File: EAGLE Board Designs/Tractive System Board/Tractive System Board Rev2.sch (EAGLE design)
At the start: 135 parts, among them J3 CONNECTOR-8_S_S, J5 CONNECTOR-4__, K4 RELAY_SPST_NC_POLARIZED_3550_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, K5 RELAY_SPST_NO_3550_12, Q2 TRANSISTOR_N_MOS__PMV15ENEA, U1 LTC6994_1, U10 DCM4623TD2J13D0T70, U11 RELAY_SOLIDSTATE_NC_AG, U15 LOGICGATE_INVERTER_DCKR, U16 LTC3639, U17 VOLTAGE_REGULATOR_ADJ_LR8_DPAK, U18 ISO224B_AIRGAP, U19 ISO224B_AIRGAP, U2 VOLTAGE_REGULATOR_SOT223_5V

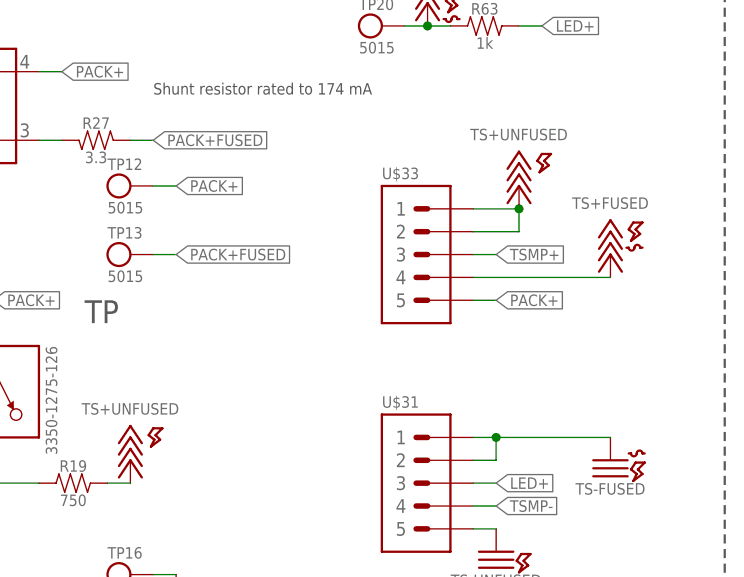
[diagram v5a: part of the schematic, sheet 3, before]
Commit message: Fixed molex connectors
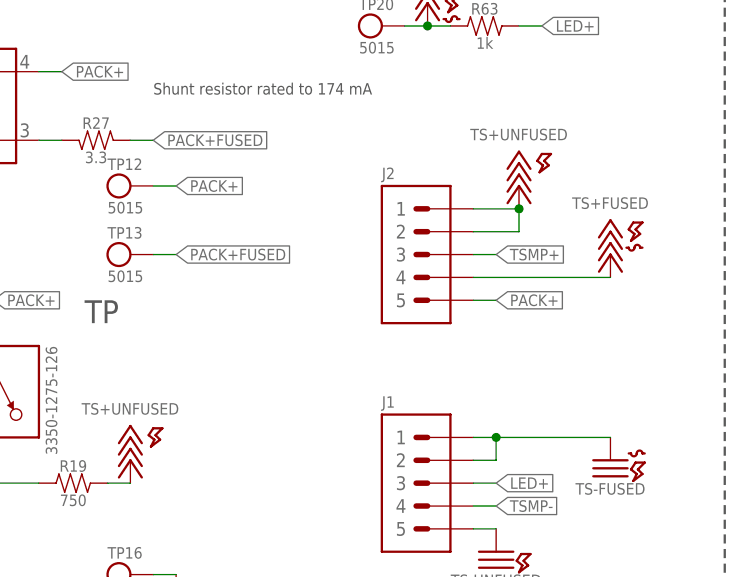
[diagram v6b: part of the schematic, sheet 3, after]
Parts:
- renumbered U$31 to J1, U$33 to J2
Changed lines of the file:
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@@
 <part name="U$3" library="HyTechSupplies" deviceset="TS-FUSED" device=""/>
 <part name="U$30" library="HyTechSupplies" deviceset="TS-FUSED" device=""/>
-<part name="U$31" library="HyTechDevices" deviceset="CONNECTOR-5_?_*" device="MICRO_V6S"/>
-<part name="U$33" library="HyTechDevices" deviceset="CONNECTOR-5_?_*" device="MICRO_V7S"/>
+<part name="J1" library="HyTechDevices" deviceset="CONNECTOR-5_?_*" device="MICRO_V6S"/>
+<part name="J2" library="HyTechDevices" deviceset="CONNECTOR-5_?_*" device="MICRO_V7S"/>
 <part name="P18" library="HyTechSupplies" deviceset="+5V" device=""/>
 <part name="TP16" library="HyTechDevices" deviceset="TEST_POINT" device=""/>
@@
 <attribute name="VALUE" x="256.54" y="147.32" size="1.27" layer="96" align="top-center"/>
 </instance>
-<instance part="U$31" gate="G$1" x="231.14" y="154.94" smashed="yes">
+<instance part="J1" gate="G$1" x="231.14" y="154.94" smashed="yes">
 <attribute name="NAME" x="231.14" y="155.702" size="1.27" layer="95"/>
 </instance>
-<instance part="U$33" gate="G$1" x="231.14" y="180.34" smashed="yes">
+<instance part="J2" gate="G$1" x="231.14" y="180.34" smashed="yes">
 <attribute name="NAME" x="231.14" y="181.102" size="1.27" layer="95"/>
 </instance>
@@
 <pinref part="P14" gate="G$1" pin="TS+UNFUSED"/>
 <wire x1="241.3" y1="177.8" x2="246.38" y2="177.8" width="0.6096" layer="91"/>
-<pinref part="U$33" gate="G$1" pin="1"/>
-<pinref part="U$33" gate="G$1" pin="2"/>
+<pinref part="J2" gate="G$1" pin="1"/>
+<pinref part="J2" gate="G$1" pin="2"/>
 <wire x1="241.3" y1="175.26" x2="246.38" y2="175.26" width="0.1524" layer="91"/>
 <wire x1="246.38" y1="175.26" x2="246.38" y2="177.8" width="0.1524" layer="91"/>
@@
 <wire x1="241.3" y1="167.64" x2="243.84" y2="167.64" width="0.6096" layer="91"/>
 <label x="243.84" y="167.64" size="1.27" layer="95" xref="yes"/>
-<pinref part="U$33" gate="G$1" pin="5"/>
+<pinref part="J2" gate="G$1" pin="5"/>
 </segment>
 <segment>
@@
 <wire x1="241.3" y1="172.72" x2="243.84" y2="172.72" width="0.6096" layer="91"/>
 <label x="243.84" y="172.72" size="1.27" layer="95" xref="yes"/>
-<pinref part="U$33" gate="G$1" pin="3"/>
+<pinref part="J2" gate="G$1" pin="3"/>
 </segment>
 <segment>
@@
 <wire x1="241.3" y1="144.78" x2="243.84" y2="144.78" width="0.6096" layer="91"/>
 <label x="243.84" y="144.78" size="1.27" layer="95" xref="yes"/>
-<pinref part="U$31" gate="G$1" pin="4"/>
+<pinref part="J1" gate="G$1" pin="4"/>
 </segment>
 <segment>
@@
 <wire x1="241.3" y1="147.32" x2="243.84" y2="147.32" width="0.6096" layer="91"/>
 <label x="243.84" y="147.32" size="1.27" layer="95" xref="yes"/>
-<pinref part="U$31" gate="G$1" pin="3"/>
+<pinref part="J1" gate="G$1" pin="3"/>
 </segment>
 <segment>
@@
 <pinref part="U$32" gate="G$1" pin="TS+FUSED"/>
 <wire x1="241.3" y1="170.18" x2="256.54" y2="170.18" width="0.6096" layer="91"/>
-<pinref part="U$33" gate="G$1" pin="4"/>
+<pinref part="J2" gate="G$1" pin="4"/>
 </segment>
 </net>
@@
 <wire x1="241.3" y1="142.24" x2="243.84" y2="142.24" width="0.6096" layer="91"/>
 <pinref part="P17" gate="G$1" pin="TS-UNFUSED"/>
-<pinref part="U$31" gate="G$1" pin="5"/>
+<pinref part="J1" gate="G$1" pin="5"/>
 </segment>
 <segment>
@@
 <wire x1="241.3" y1="152.4" x2="243.84" y2="152.4" width="0.6096" layer="91"/>
 <pinref part="U$30" gate="G$1" pin="TS-FUSED"/>
-<pinref part="U$31" gate="G$1" pin="1"/>
-<pinref part="U$31" gate="G$1" pin="2"/>
+<pinref part="J1" gate="G$1" pin="1"/>
+<pinref part="J1" gate="G$1" pin="2"/>
 <wire x1="243.84" y1="152.4" x2="256.54" y2="152.4" width="0.6096" layer="91"/>
 <wire x1="241.3" y1="149.86" x2="243.84" y2="149.86" width="0.6096" layer="91"/>
